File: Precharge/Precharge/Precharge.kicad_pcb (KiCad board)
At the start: 2 copper layers, 104 parts, among them J1 MicroFit, J2 HV, K1 OMRON-G2R-24, K2 G7L-2A-X-L, Q1 2N7002, Q2 MMBT3906, Q3 2N7002, U1 SPAN02A-12, U10 4N35, U2 Teensy4.0, U3 LM1117-5.0, U4 4N35, U5 4N35, U6 LM331, U7 LM331, U8 LM2904, U9 LM393

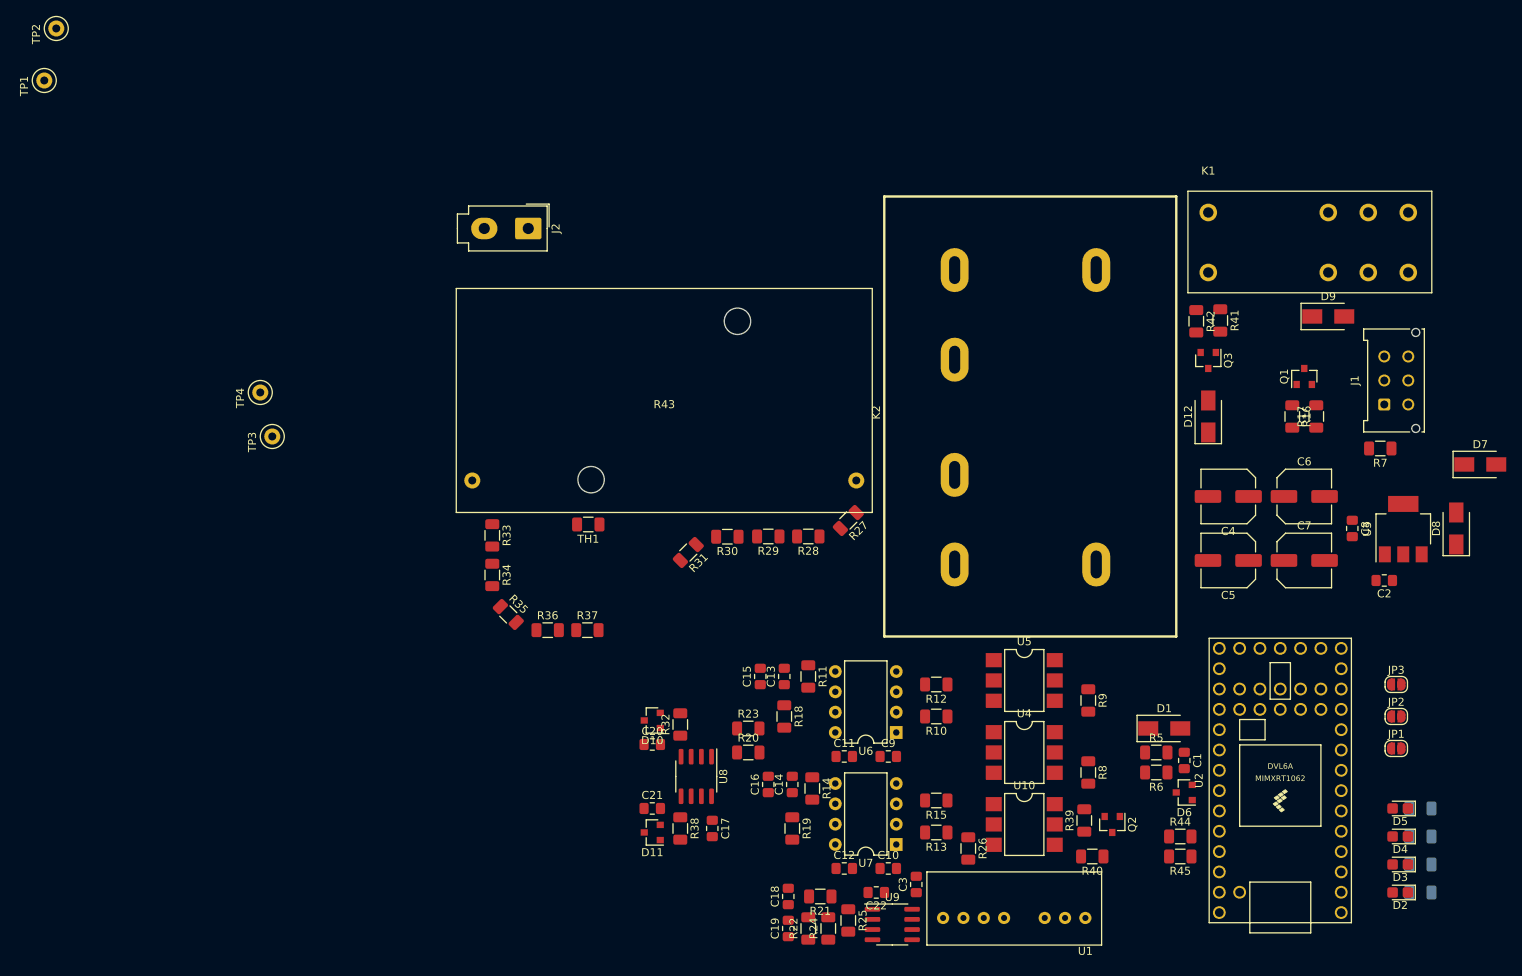
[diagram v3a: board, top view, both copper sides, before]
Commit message: :hammer: position components, add CAD models
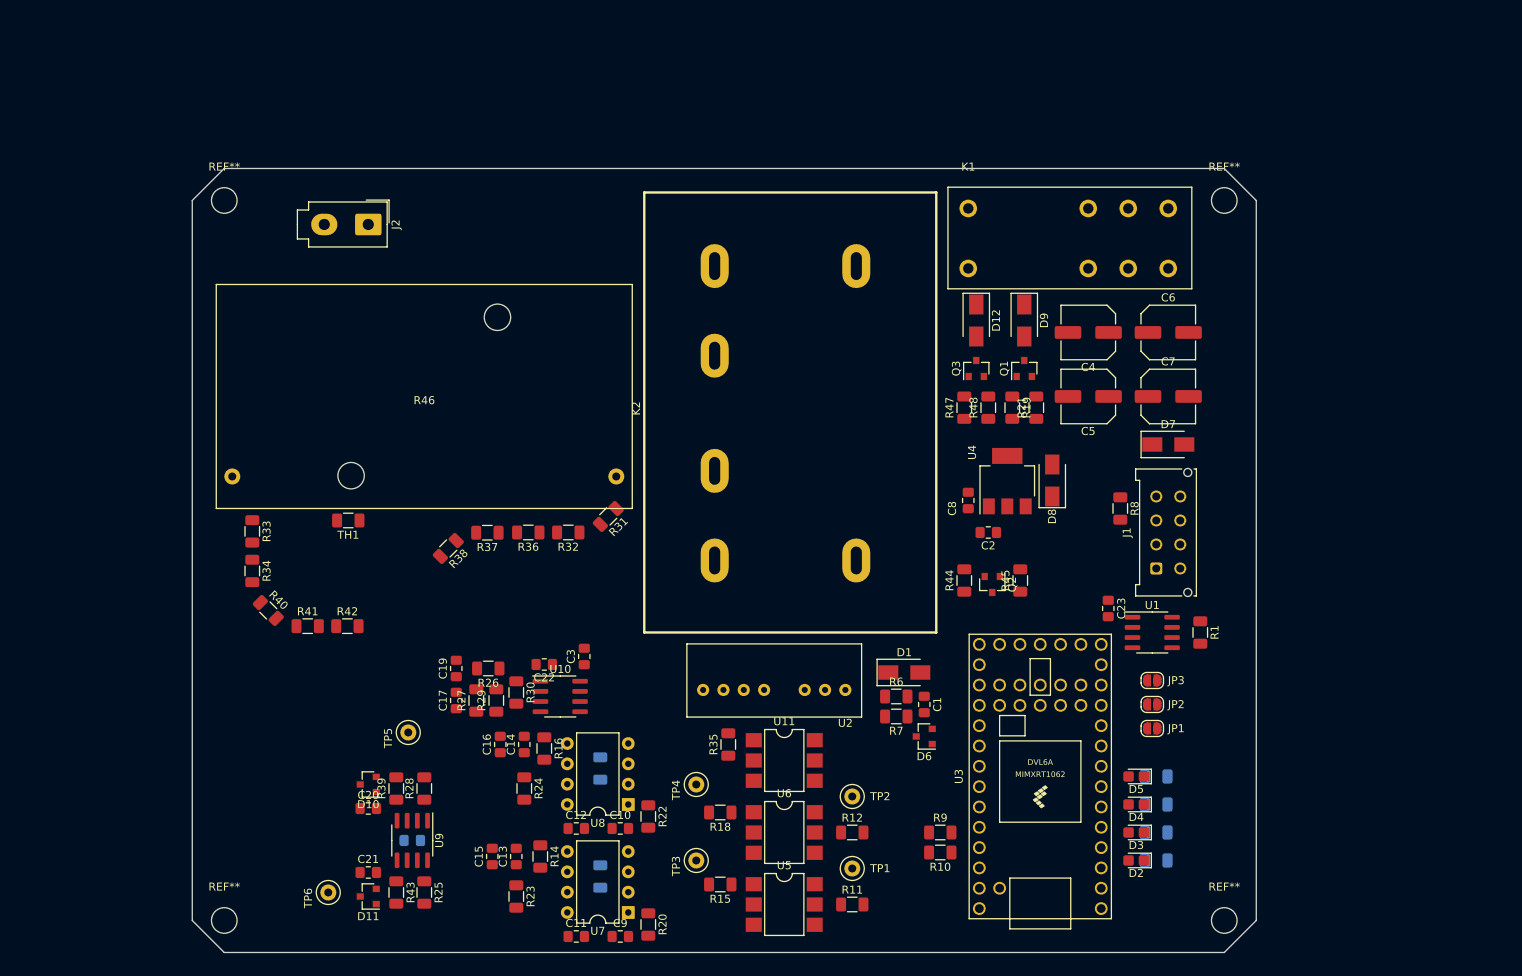
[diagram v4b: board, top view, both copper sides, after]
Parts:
- added C23: 100n, Capacitor_SMD:C_0805_2012Metric_Pad1.15x1.40mm_HandSolder, F.Cu at (182.5, 105.5)
- added R1: 160, Resistor_SMD:R_1206_3216Metric, F.Cu at (194.0, 108.5)
- added R20: 100k, Resistor_SMD:R_1206_3216Metric, F.Cu at (125.0, 145.0)
- added R22: 100k, Resistor_SMD:R_1206_3216Metric, F.Cu at (125.0, 131.5)
- added REF**: MountingHole_3.2mm_M3, MountingHole:MountingHole_3.2mm_M3, F.Cu at (72.0, 144.5)
- added REF**: MountingHole_3.2mm_M3, MountingHole:MountingHole_3.2mm_M3, F.Cu at (72.0, 54.5)
- added REF**: MountingHole_3.2mm_M3, MountingHole:MountingHole_3.2mm_M3, F.Cu at (197.0, 54.5)
- added REF**: MountingHole_3.2mm_M3, MountingHole:MountingHole_3.2mm_M3, F.Cu at (197.0, 144.5)
- added TP1: TestPoint, TestPoint:TestPoint_Loop_D2.50mm_Drill1.0mm_LowProfile, F.Cu at (150.5, 138.0)
- added TP2: TestPoint, TestPoint:TestPoint_Loop_D2.50mm_Drill1.0mm_LowProfile, F.Cu at (150.5, 129.0)
- added U1: TJA1051T-3, Package_SO:SOIC-8_3.9x4.9mm_P1.27mm, F.Cu at (188.0, 108.5)
- C18: renamed from C17; moved to B.Cu
- J1: footprint Connector_Molex:Molex_Micro-Fit_3.0_43045-0612_2x03_P3.00mm_Vertical -> Connector_Molex:Molex_Micro-Fit_3.0_43045-0812_2x04_P3.00mm_Vertical
- R11: renamed from R8; value 1k -> 1k5
- R12: renamed from R9; value 1k -> 1k5
- R13: renamed from R10; value Rs -> 12k; moved to B.Cu
- R15: renamed from R12; value 470 -> 560
- R17: renamed from R13; value Rs -> 12k; moved to B.Cu
- R18: renamed from R15; value 470 -> 560
- R23: renamed from R18; value 6k8 -> 10k
- R24: renamed from R19; value 6k8 -> 10k
- R35: renamed from R26; value 470 -> 560
- R44: renamed from R39; value 470 -> 10k
- R46: renamed from R43; value R -> HSA25390RJ
- moved TP3 127.1 mm to (131.0, 137.0)
- moved TP4 123.8 mm to (131.0, 127.5)
- moved TP6 63.1 mm to (85.0, 141.0)
- moved D8 50.9 mm to (175.5, 89.5)
- moved C17 50.3 mm to (101.0, 117.0)
- moved C19 50.3 mm to (101.0, 113.0)
- moved C22 50.3 mm to (112.0, 112.5)
- moved C3 50.3 mm to (117.0, 111.5)
- moved R26 50.3 mm to (105.0, 113.0)
- moved R27 50.3 mm to (103.5, 117.0)
- moved R29 50.3 mm to (106.0, 117.0)
- moved R30 50.3 mm to (108.5, 116.0)
- moved U10 50.3 mm to (114.0, 116.5)
- moved C2 49.9 mm to (167.5, 96.0)
- moved U4 49.9 mm to (169.9, 89.6)
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- renumbered C19 to C17, C18 to C19, R45 to R10, R11 to R14, R14 to R16, R16 to R19, R1 to R2, R17 to R21, R20 to R25, R21 to R26, R22 to R27, R23 to R28, R24 to R29, R2 to R3, R25 to R30, R27 to R31, R28 to R32, R29 to R36, R30 to R37, R31 to R38, R32 to R39, R3 to R4, R35 to R40, R36 to R41, R37 to R42, R38 to R43, R40 to R45, R41 to R47, R42 to R48, R4 to R5, R5 to R6, R6 to R7, R7 to R8, R44 to R9, TP1 to TP3, TP2 to TP4, TP3 to TP5, TP4 to TP6, U9 to U10, U10 to U11, U1 to U2, U2 to U3, U3 to U4, U4 to U5, U5 to U6, U6 to U7, U7 to U8, U8 to U9
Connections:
- C17 pad 1: Net-(C19-Pad1) (its old number) -> +12P
- C17 pad 2: GNDS -> Net-(C17-Pad2)
- JP1 pad 1: (no net) -> /CFG0
- JP2 pad 1: (no net) -> /CFG1
- JP3 pad 1: (no net) -> /CFG2
- R11 pad 1: GLV- -> /Fts
- R11 pad 2: /Fts -> +3V3
- R12 pad 1: GLV- -> /Faccu
- R12 pad 2: /Faccu -> +3V3
- R14 pad 2: Net-(C9-Pad1) -> Net-(C9-Pad2)
- R16 pad 2: Net-(C10-Pad1) -> Net-(C10-Pad2)
- R19 pad 2: (no net) -> /SHTDN_CTRL
- R29 pad 1: Net-(C19-Pad1) (its old number) -> Net-(C17-Pad2)
- R44 pad 1: Net-(R39-Pad1) -> Net-(Q2-Pad1)
- R44 pad 2: Net-(Q2-Pad1) -> +12V
- R47 pad 1: (no net) -> /PRECHG
- TH1 pad 1: Net-(C19-Pad1) (its old number) -> Net-(C17-Pad2)
- U10 pad 2: Net-(C19-Pad1) (its old number) -> Net-(C17-Pad2)
- U11 pad 5: Net-(R39-Pad1) -> Net-(Q2-Pad1)
- U3 pad 10: (no net) -> /CANTX
- U3 pad 13: (no net) -> /SHTDN_CTRL
- U3 pad 14: (no net) -> /PRECHG
- U3 pad 21: (no net) -> /Faccu
- U3 pad 22: (no net) -> /Fts
- U3 pad 6: (no net) -> /CFG0
- U3 pad 7: (no net) -> /CFG1
- U3 pad 8: (no net) -> /CFG2
- U3 pad 9: (no net) -> /CANRX
- U5 pad 4: /Fts -> GLV-
- U5 pad 5: +3V3 -> /Fts
- U6 pad 4: /Faccu -> GLV-
- U6 pad 5: +3V3 -> /Faccu
- U7 pad 1: Net-(C9-Pad2) -> Net-(C9-Pad1)
- U8 pad 1: Net-(C10-Pad2) -> Net-(C10-Pad1)
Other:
- board outline added: 133 x 98 mm

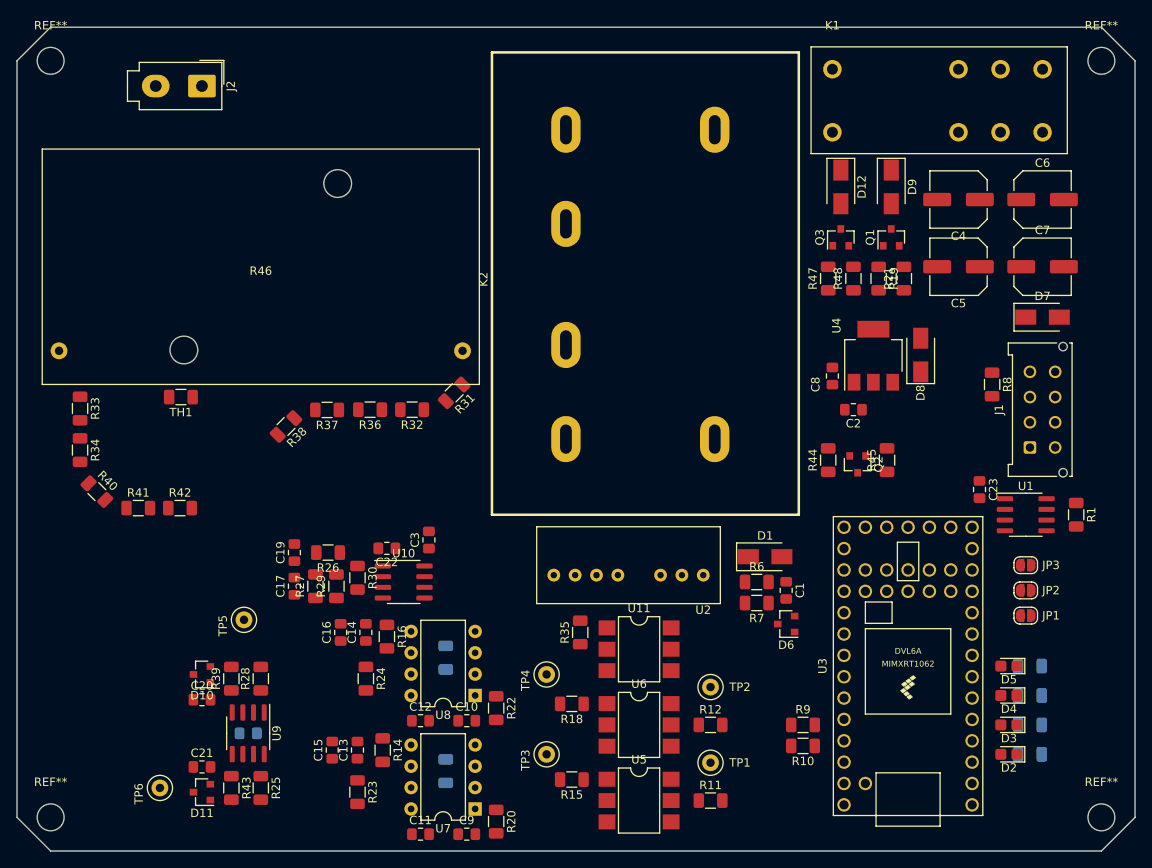
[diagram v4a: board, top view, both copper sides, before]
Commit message: :hourglass_flowing_sand: hand-route crucial sections
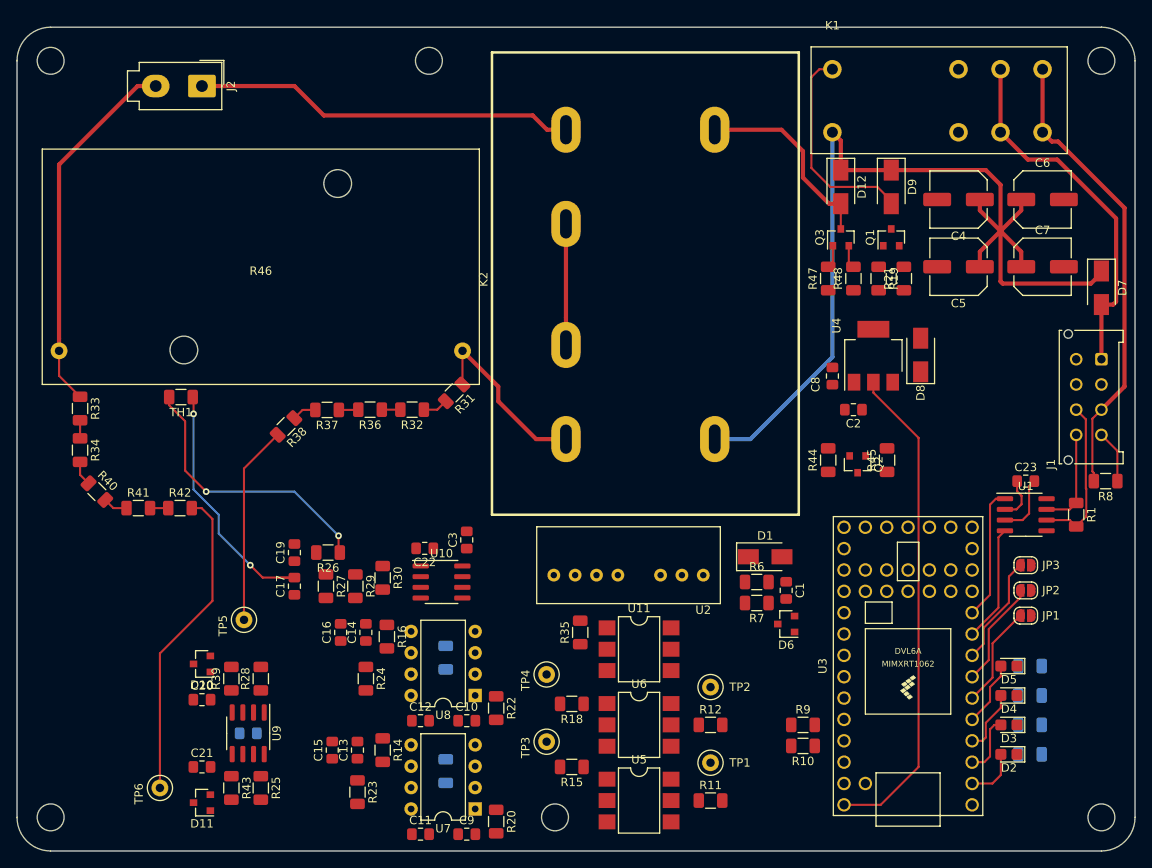
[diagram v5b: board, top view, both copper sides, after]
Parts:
- removed REF** (x4): MountingHole_3.2mm_M3, MountingHole:MountingHole_3.2mm_M3
- added MT1: MountingHole_3.2mm_M3, MountingHole:MountingHole_3.2mm_M3, F.Cu at (72.0, 144.5)
- added MT2: MountingHole_3.2mm_M3, MountingHole:MountingHole_3.2mm_M3, F.Cu at (197.0, 144.5)
- added MT3: MountingHole_3.2mm_M3, MountingHole:MountingHole_3.2mm_M3, F.Cu at (132.0, 144.5)
- added MT4: MountingHole_3.2mm_M3, MountingHole:MountingHole_3.2mm_M3, F.Cu at (117.0, 54.5)
- added MT5: MountingHole_3.2mm_M3, MountingHole:MountingHole_3.2mm_M3, F.Cu at (197.0, 54.5)
- added MT6: MountingHole_3.2mm_M3, MountingHole:MountingHole_3.2mm_M3, F.Cu at (72.0, 54.5)
- K1: value OMRON-G2R-24 -> OMRON-G2RL-24
- moved R8 17.7 mm to (197.5, 104.5), turned to 180 degrees
- moved J1 13.5 mm to (197.0, 90.0), turned to 270 degrees
- moved D7 7.83 mm to (197.0, 81.5), turned to 270 degrees
- moved C23 5.59 mm to (188.0, 104.5), turned to 0 degrees
- moved C22 4.50 mm to (116.5, 112.5)
- moved C3 4.50 mm to (121.5, 111.5)
- moved U10 4.50 mm to (118.5, 116.5)
- moved R30 3.00 mm to (111.5, 116.0)
- moved R29 2.25 mm to (108.2, 117.0), turned to 270 degrees
- moved R15 1.50 mm to (134.0, 138.5)
- moved TP3 1.50 mm to (131.0, 135.5)
- moved D10 1.25 mm to (90.0, 126.2)
- moved D11 1.25 mm to (90.0, 142.8)
- moved R27 1.25 mm to (104.8, 117.0), turned to 270 degrees
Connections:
- J1 pad 2: GLV- -> (no net)
- J1 pad 5: /PDOC_OK -> GLV-
- J1 pad 6: (no net) -> /PDOC_OK
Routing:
- net +12V: track 0.00 -> 114.3 mm
- net +5V: track 0.00 -> 66.0 mm
- net /SHTDN_OUT: track 0.00 -> 55.1 mm
- net Net-(J2-Pad1): track 0.00 -> 45.5 mm
- net /VinTS: track 0.00 -> 44.0 mm
- net GLV+: track 0.00 -> 43.8 mm
- net Net-(C21-Pad1): track 0.00 -> 37.6 mm
- net +12P: track 0.00 -> 33.1 mm, vias 0 -> 2
- net Net-(C17-Pad2): track 0.00 -> 30.7 mm, vias 0 -> 2
- net Net-(D9-Pad2): track 0.00 -> 25.2 mm
- net Net-(C20-Pad1): track 0.00 -> 23.7 mm
- net Net-(D12-Pad2): track 0.00 -> 23.5 mm
- net /VinAccu: track 0.00 -> 21.7 mm
- net /CANL: track 0.00 -> 18.7 mm
- net /CANTX: track 0.00 -> 15.8 mm
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
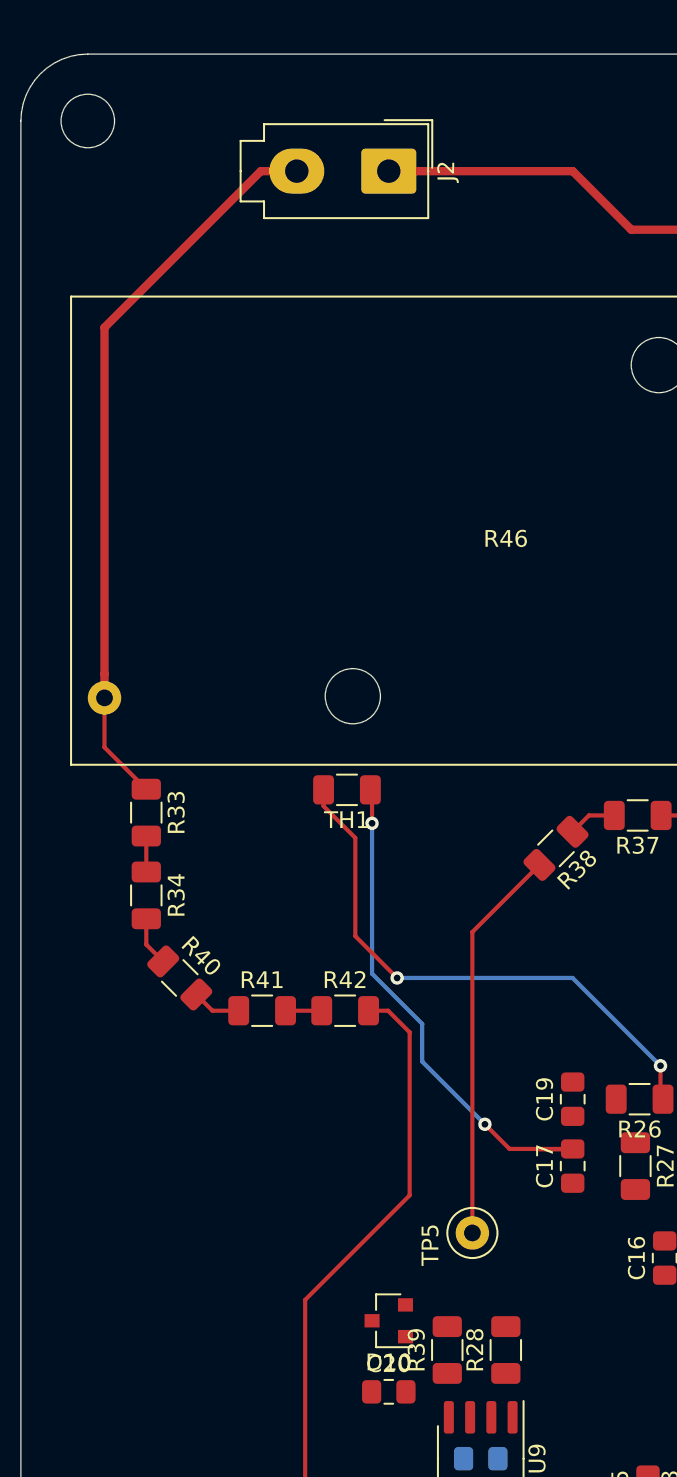
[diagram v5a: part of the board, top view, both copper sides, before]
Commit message: :pencil: Add connector cad files and associate with footprints.
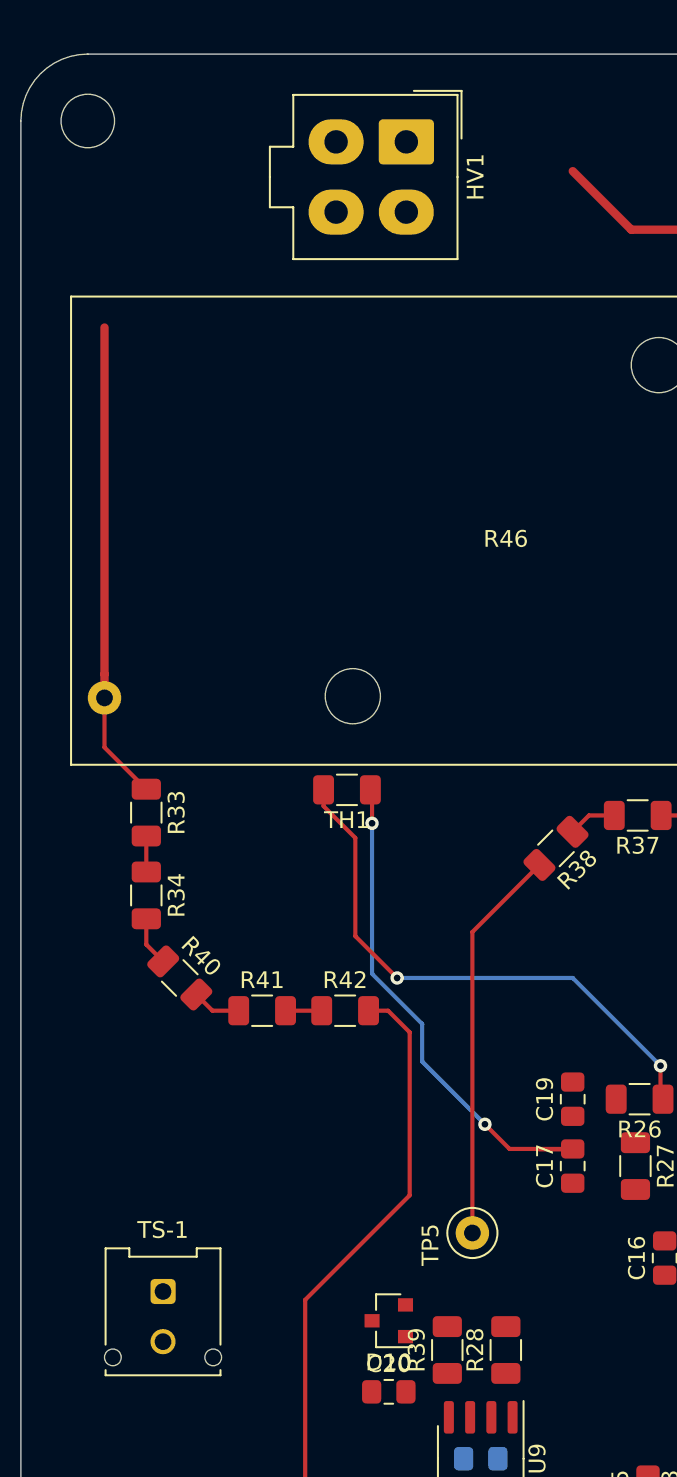
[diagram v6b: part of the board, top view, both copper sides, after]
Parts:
- added TS-1: Micro-Fit 43045-0212, Connector_Molex:Molex_Micro-Fit_3.0_43045-0212_2x01_P3.00mm_Vertical, F.Cu at (76.5, 124.5)
- HV1: renamed from J2; value HV -> Mini-Fit_Jr_5566-04A; footprint Connector_Molex:Molex_Mini-Fit_Jr_5566-02A_2x01_P4.20mm_Vertical -> Mini-Fit-Jr-4.20mm-pitch:Molex-Mini-Fit-Jr-4-pin-P4.2mm-RowP4.2mm
- moved HV1 2.47 mm to (91.8, 55.8)
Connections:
- HV1 pad 2: /VinTS -> (no net)
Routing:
- net /VinTS: track 44.0 -> 28.6 mm
- net Net-(HV1-Pad1): track 45.5 -> 34.5 mm
